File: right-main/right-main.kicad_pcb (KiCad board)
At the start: 2 copper layers, 150.4 x 123.8 mm, 209 parts, among them J1 USBCONN, P1 CONN_4, P2 CONN_5, P3 CONN_6, SW1 PTS525SM10, SW11 SPST, SW12 SPST, SW13 SPST, SW14 SPST, SW15 SPST, SW16 SPST, SW17 SPST, SW21 SPST, SW22 SPST, SW23 SPST, SW24 SPST, SW25 SPST, SW26 SPST, SW27 SPST, SW31 SPST, SW32 SPST, SW33 SPST, SW34 SPST, SW35 SPST, SW36 SPST, SW37 SPST, SW41 SPST, SW42 SPST, SW43 SPST, SW44 SPST, SW45 SPST, SW46 SPST, SW47 SPST, SW52 SPST, SW53 SPST, SW54 SPST, SW55 SPST, SW56 SPST, SW57 SPST, U1 ATMEGA32U4, U2 CAT24C256, X1 16Mhz

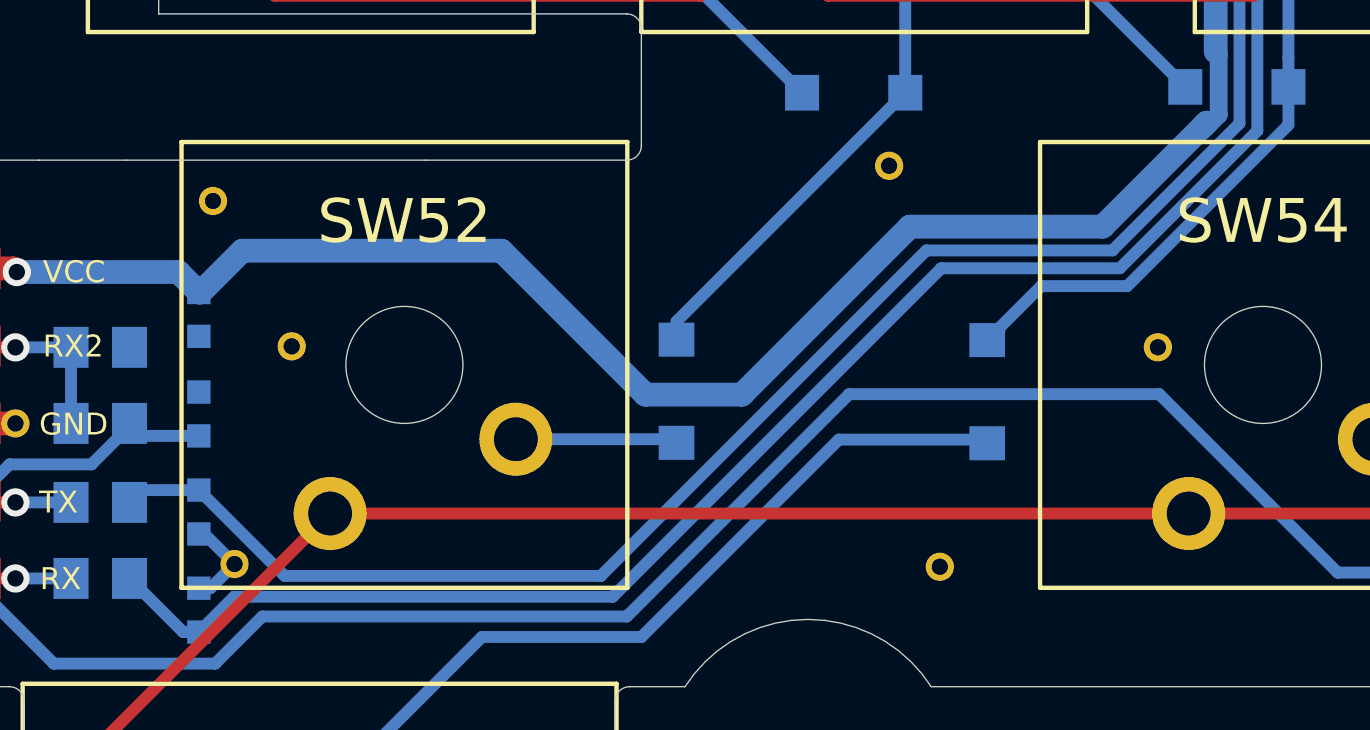
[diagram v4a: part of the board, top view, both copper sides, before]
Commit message: switch 52 right
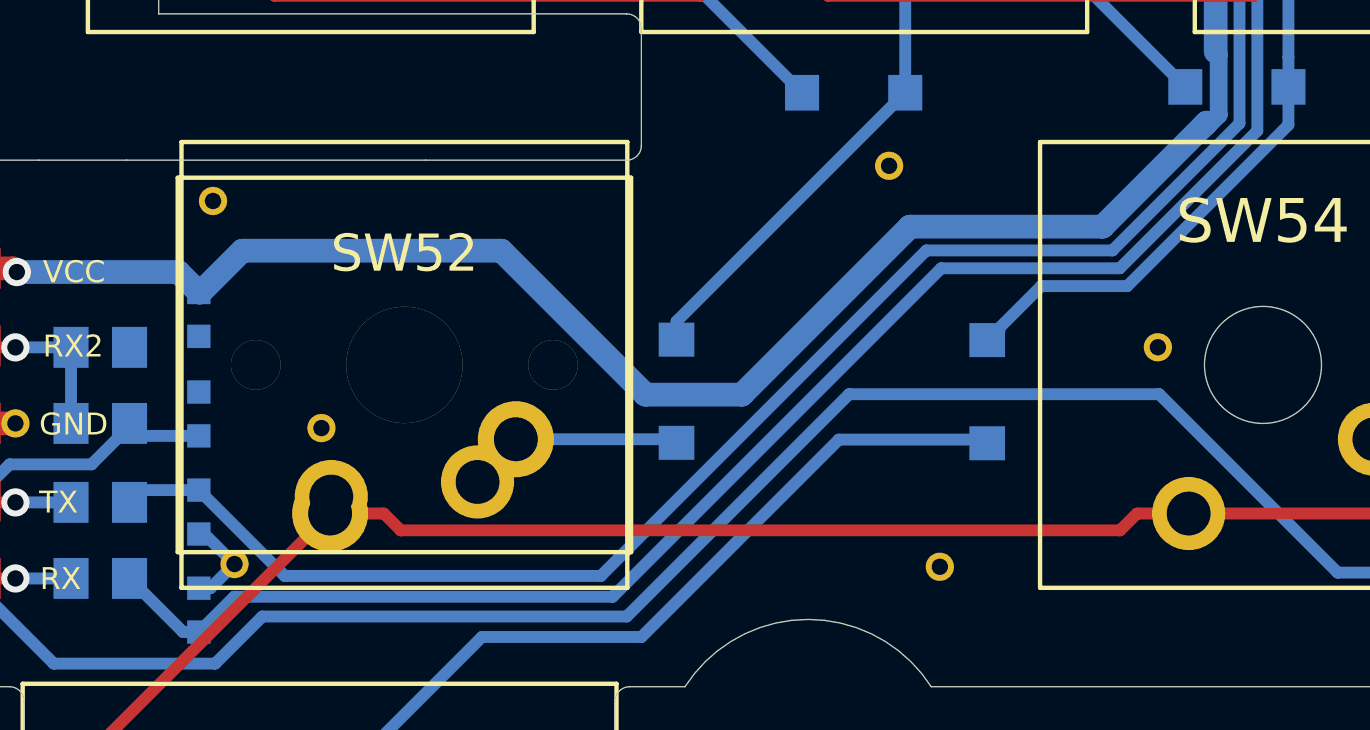
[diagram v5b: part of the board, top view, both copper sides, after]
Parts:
- SW52: footprint UGL:Cherry_MX -> ugl:Cherry-MX-Matias-Hybrid
- moved via 38/22mil 2.97 mm to (131.1, 141.9)
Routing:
- net Net-(D52-Pad2): track 5.65 -> 7.66 mm
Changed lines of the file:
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@@
 (kicad_pcb (version 4) (host pcbnew 4.0.1-stable)
   (general
-    (links 363)
+    (links 365)
     (no_connects 0)
-    (area 19.803 18.9051 270.000001 165.000001)
+    (area 109.795002 32.293387 260.205001 156.105002)
     (thickness 1.6)
     (drawings 354)
-    (tracks 1122)
+    (tracks 1128)
     (zones 0)
     (modules 209)
@@
   )
   (layers
-    (0 F.Cu signal hide)
-    (31 B.Cu signal)
+    (0 F.Cu signal)
+    (31 B.Cu signal hide)
     (32 B.Adhes user)
     (33 F.Adhes user)
@@
   )
   (setup
-    (last_trace_width 0.6096)
+    (last_trace_width 0.4064)
     (user_trace_width 0.2032)
     (user_trace_width 0.3048)
@@
   )
   (module UGL:via_38_22mil (layer F.Cu)
-    (at 130.048 139.065)
+    (at 131.064 141.859)
     (fp_text reference "via 38/22mil" (at 0 -1.8) (layer F.SilkS) hide
       (effects (font (size 0.75 0.75) (thickness 0.15)))
@@
       (net 20 /ROW5))
   )
-  (module UGL:Cherry_MX locked (layer F.Cu)
-    (at 133.899997 139.7 180)
-    (fp_text reference SW52 (at 0 4.9 180) (layer F.SilkS)
-      (effects (font (size 1.5 1.5) (thickness 0.3)))
-    )
-    (fp_text value SPST (at 0 0 180) (layer F.SilkS) hide
-      (effects (font (size 1.5 1.5) (thickness 0.3)))
-    )
-    (fp_line (start -7.6 -7.6) (end -7.6 7.6) (layer B.SilkS) (width 0.15))
-    (fp_line (start -7.6 7.6) (end 7.6 7.6) (layer B.SilkS) (width 0.15))
-    (fp_line (start 7.6 -7.6) (end 7.6 7.6) (layer B.SilkS) (width 0.15))
-    (fp_line (start -7.6 -7.6) (end 7.6 -7.6) (layer B.SilkS) (width 0.15))
-    (fp_line (start -7.62 -7.62) (end 7.62 -7.62) (layer F.SilkS) (width 0.15))
-    (fp_line (start 7.62 -7.62) (end 7.62 7.62) (layer F.SilkS) (width 0.15))
-    (fp_line (start 7.62 7.62) (end -7.62 7.62) (layer F.SilkS) (width 0.15))
-    (fp_line (start -7.62 7.62) (end -7.62 -7.62) (layer F.SilkS) (width 0.15))
-    (pad "" np_thru_hole circle (at 0 0 180) (size 4 4) (drill 4) (layers *.Cu *.Mask F.SilkS))
-    (pad 2 thru_hole circle (at -3.81 -2.54 180) (size 2.5 2.5) (drill 1.5) (layers *.Cu *.Mask F.SilkS)
-      (net 58 "Net-(D52-Pad2)"))
-    (pad 1 thru_hole circle (at 2.54 -5.08 180) (size 2.5 2.5) (drill 1.5) (layers *.Cu *.Mask F.SilkS)
-      (net 20 /ROW5))
-  )
   (module UGL:UX60-MB-5S8 locked (layer F.Cu)
     (at 175.849803 43.601924 85.4)
@@
     )
   )
+  (module ugl:Cherry-MX-Matias-Hybrid locked (layer F.Cu)
+    (at 133.899997 139.7 180)
+    (tags switch)
+    (fp_text reference SW52 (at 0 3.81 180) (layer F.SilkS)
+      (effects (font (thickness 0.3048)))
+    )
+    (fp_text value SPST (at 0 0 180) (layer F.SilkS) hide
+      (effects (font (thickness 0.3048)))
+    )
+    (fp_line (start -7.62 7.62) (end -7.62 -7.62) (layer B.SilkS) (width 0.15))
+    (fp_line (start 7.62 7.62) (end -7.62 7.62) (layer B.SilkS) (width 0.15))
+    (fp_line (start 7.62 -7.62) (end 7.62 7.62) (layer B.SilkS) (width 0.15))
+    (fp_line (start -7.62 -7.62) (end 7.62 -7.62) (layer B.SilkS) (width 0.15))
+    (fp_line (start -7.75 -6.4) (end -7.75 6.4) (layer F.SilkS) (width 0.15))
+    (fp_line (start 7.75 -6.4) (end 7.75 6.4) (layer F.SilkS) (width 0.15))
+    (fp_line (start -7.75 6.4) (end 7.75 6.4) (layer F.SilkS) (width 0.15))
+    (fp_line (start -7.75 -6.4) (end 7.75 -6.4) (layer F.SilkS) (width 0.15))
+    (fp_line (start -7.62 -7.62) (end 7.62 -7.62) (layer F.SilkS) (width 0.15))
+    (fp_line (start 7.62 -7.62) (end 7.62 7.62) (layer F.SilkS) (width 0.15))
+    (fp_line (start 7.62 7.62) (end -7.62 7.62) (layer F.SilkS) (width 0.15))
+    (fp_line (start -7.62 7.62) (end -7.62 -7.62) (layer F.SilkS) (width 0.15))
+    (pad 0 thru_hole circle (at 0 0 180) (size 3.98018 3.98018) (drill 3.98018) (layers *.Cu *.Mask F.SilkS))
+    (pad 1 thru_hole circle (at 2.54 -5.08 180) (size 2.6 2.6) (drill 1.5011) (layers *.Cu *.Mask F.SilkS)
+      (net 20 /ROW5))
+    (pad 2 thru_hole circle (at -3.81 -2.54 180) (size 2.6 2.6) (drill 1.5011) (layers *.Cu *.Mask F.SilkS)
+      (net 58 "Net-(D52-Pad2)"))
+    (pad "" thru_hole circle (at -5.08 0 180) (size 1.69926 1.69926) (drill 1.69926) (layers *.Cu *.Mask F.SilkS))
+    (pad "" thru_hole circle (at 5.08 0 180) (size 1.69926 1.69926) (drill 1.69926) (layers *.Cu *.Mask F.SilkS))
+    (pad 1 thru_hole circle (at 2.5 -4.5 180) (size 2.5 2.5) (drill 1.5) (layers *.Cu *.Mask F.SilkS)
+      (net 20 /ROW5))
+    (pad 2 thru_hole circle (at -2.5 -4 180) (size 2.5 2.5) (drill 1.5) (layers *.Cu *.Mask F.SilkS)
+      (net 58 "Net-(D52-Pad2)"))
+    (model cherry_mx1.wrl
+      (at (xyz 0 0 0))
+      (scale (xyz 1 1 1))
+      (rotate (xyz 0 0 0))
+    )
+  )
   (gr_line (start 120.857 138.196) (end 121.657 137.396) (angle 90) (layer B.SilkS) (width 0.2))
   (gr_line (start 124.457 148.096) (end 124.457 148.296) (angle 90) (layer B.SilkS) (width 0.2))
@@
   (segment (start 241.06 124.899) (end 241.06 123.24) (width 0.4064) (layer B.Cu) (net 19))
   (segment (start 246.257 130.096) (end 241.06 124.899) (width 0.4064) (layer B.Cu) (net 19))
+  (segment (start 160.710003 144.78) (end 158.942237 144.78) (width 0.4064) (layer F.Cu) (net 20))
+  (segment (start 158.942237 144.78) (end 158.365836 145.356401) (width 0.4064) (layer F.Cu) (net 20))
+  (segment (start 158.365836 145.356401) (end 133.774875 145.356401) (width 0.4064) (layer F.Cu) (net 20))
+  (segment (start 133.774875 145.356401) (end 133.198474 144.78) (width 0.4064) (layer F.Cu) (net 20))
+  (segment (start 133.198474 144.78) (end 131.359997 144.78) (width 0.4064) (layer F.Cu) (net 20))
   (segment (start 212.503 128.9936) (end 212.503 130.1) (width 0.4064) (layer B.Cu) (net 20))
   (segment (start 213.115622 128.380978) (end 212.503 128.9936) (width 0.4064) (layer B.Cu) (net 20))
@@
   (segment (start 207.509998 144.78) (end 184.109997 144.78) (width 0.4064) (layer F.Cu) (net 20))
   (segment (start 184.109997 144.78) (end 160.710003 144.78) (width 0.4064) (layer F.Cu) (net 20))
-  (segment (start 160.710003 144.78) (end 131.359997 144.78) (width 0.4064) (layer F.Cu) (net 20))
   (segment (start 122.950003 153.189994) (end 122.950003 153.8) (width 0.4064) (layer F.Cu) (net 20))
   (segment (start 131.359997 144.78) (end 122.950003 153.189994) (width 0.4064) (layer F.Cu) (net 20))
@@
   (segment (start 234.71 125.78) (end 234.1647 126.3253) (width 0.4064) (layer B.Cu) (net 57))
   (segment (start 234.1647 126.3253) (end 234.1647 130.1) (width 0.4064) (layer B.Cu) (net 57))
+  (segment (start 136.399997 143.7) (end 136.399997 143.55) (width 0.4064) (layer B.Cu) (net 58))
+  (segment (start 136.399997 143.55) (end 137.709997 142.24) (width 0.4064) (layer B.Cu) (net 58))
   (segment (start 143.3449 142.24) (end 143.3576 142.2527) (width 0.4064) (layer B.Cu) (net 58))
   (segment (start 137.709997 142.24) (end 143.3449 142.24) (width 0.4064) (layer B.Cu) (net 58))
